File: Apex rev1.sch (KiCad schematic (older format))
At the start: 17 parts, among them J1 OLED, SW1 SW_PUSH, SW2 Rotary_Encoder, U1 AT90USB1286-MU, Y1 8MHz

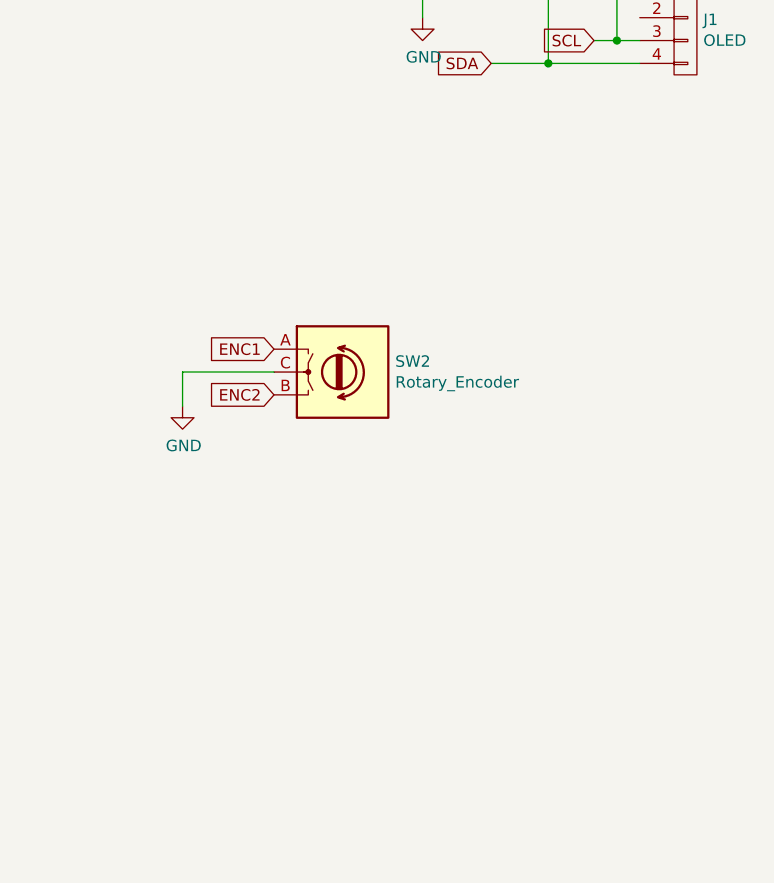
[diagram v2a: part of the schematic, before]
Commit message: Associate FP
added debounce to encoder. finalized footrpint association.
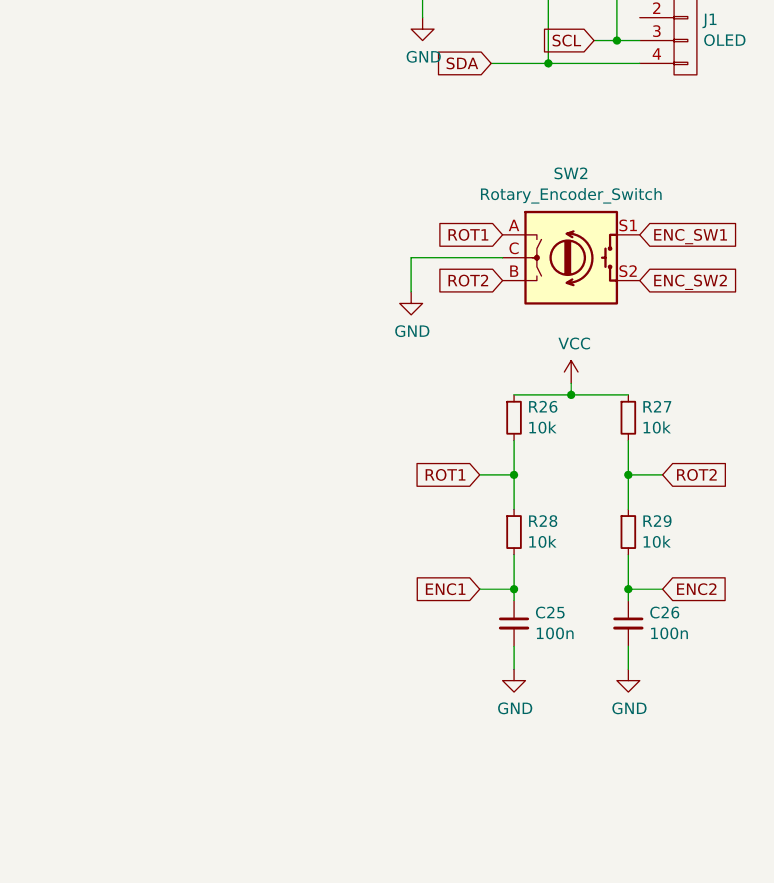
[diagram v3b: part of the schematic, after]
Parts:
- removed SW2: Rotary_Encoder, symbol Device:Rotary_Encoder
- added C25, C26: 100n, Capacitor_SMD:C_0805_2012Metric, symbol Device:C_Small
- added R26, R27, R28, R29: 10k, 1_Keyboard Footprints:R_0603, symbol Device:R_Small
- added SW2: Rotary_Encoder_Switch, 1_Keyboard Footprints:RotaryEncoder_EC11, symbol Device:Rotary_Encoder_Switch
- J1: footprint (none) -> hub_keyboard:128X32_I2C_OLED
- R1, R2, R3, R4: footprint (none) -> 1_Keyboard Footprints:R_0603
- SW1: footprint (none) -> 1_Keyboard Footprints:SKQG-1155865
- Y1: footprint (none) -> Crystal:Crystal_SMD_0603-2Pin_6.0x3.5mm
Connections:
- net ENC1: now also C25.1, R28.2
- net ENC2: now also C26.1, R29.2
- net GND: now also C25.2, C26.2, R26.1, R27.1, SW2.C
- new net ENC_SW1: SW2.S1
- new net ENC_SW2: SW2.S2
- new net ROT1: R26.2, R28.1, SW2.A
- new net ROT2: R27.2, R29.1, SW2.B
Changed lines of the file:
@@
 F 0 "R3" H 8321 1546 50  0000 L CNN
 F 1 "10k" H 8321 1455 50  0000 L CNN
-F 2 "" H 8250 1500 60  0001 C CNN
+F 2 "1_Keyboard Footprints:R_0603" H 8250 1500 60  0001 C CNN
 F 3 "" H 8250 1500 60  0000 C CNN
 	1    8250 1500
@@
 F 0 "SW1" H 7800 2005 50  0000 C CNN
 F 1 "SW_PUSH" H 7800 1914 50  0000 C CNN
-F 2 "" H 7800 1750 60  0001 C CNN
+F 2 "1_Keyboard Footprints:SKQG-1155865" H 7800 1750 60  0001 C CNN
 F 3 "" H 7800 1750 60  0000 C CNN
 	1    7800 1750
@@
 F 0 "Y1" V 7904 2181 50  0000 L CNN
 F 1 "8MHz" V 7995 2181 50  0000 L CNN
-F 2 "" H 7950 2050 50  0001 C CNN
+F 2 "Crystal:Crystal_SMD_0603-2Pin_6.0x3.5mm" H 7950 2050 50  0001 C CNN
 F 3 "~" H 7950 2050 50  0001 C CNN
 	1    7950 2050
@@
 F 0 "R4" H 8220 4096 50  0000 L CNN
 F 1 "1k" H 8220 4005 50  0000 L CNN
-F 2 "" V 8080 4050 50  0001 C CNN
+F 2 "1_Keyboard Footprints:R_0603" V 8080 4050 50  0001 C CNN
 F 3 "~" H 8150 4050 50  0001 C CNN
 	1    8150 4050
@@
 F 0 "J1" H 13278 1491 50  0000 L CNN
 F 1 "OLED" H 13278 1400 50  0000 L CNN
-F 2 "" H 13200 1450 50  0001 C CNN
+F 2 "hub_keyboard:128X32_I2C_OLED" H 13200 1450 50  0001 C CNN
 F 3 "" H 13200 1450 50  0000 C CNN
 	1    13200 1450
@@
 F 0 "R1" H 12670 1096 50  0000 L CNN
 F 1 "20k" H 12670 1005 50  0000 L CNN
-F 2 "" V 12530 1050 50  0001 C CNN
+F 2 "1_Keyboard Footprints:R_0603" V 12530 1050 50  0001 C CNN
 F 3 "~" H 12600 1050 50  0001 C CNN
 	1    12600 1050
@@
 F 0 "R2" H 12970 1096 50  0000 L CNN
 F 1 "20k" H 12970 1005 50  0000 L CNN
-F 2 "" V 12830 1050 50  0001 C CNN
+F 2 "1_Keyboard Footprints:R_0603" V 12830 1050 50  0001 C CNN
 F 3 "~" H 12900 1050 50  0001 C CNN
 	1    12900 1050
@@
 	1    0    0    -1
 $EndComp
-$Comp
-L Device:Rotary_Encoder SW2
-U 1 1 5F0786F9
-P 11700 2950
-F 0 "SW2" H 11930 2996 50  0000 L CNN
-F 1 "Rotary_Encoder" H 11930 2905 50  0000 L CNN
-F 2 "" H 11550 3110 50  0001 C CNN
-F 3 "~" H 11700 3210 50  0001 C CNN
-	1    11700 2950
-	1    0    0    -1
-$EndComp
-Text GLabel 11400 2850 0    50   Input ~ 0
-ENC1
-Text GLabel 11400 3050 0    50   Input ~ 0
-ENC2
-Wire Wire Line
-	11400 2950 11000 2950
-Wire Wire Line
-	11000 2950 11000 3100
+Text GLabel 12400 2350 0    50   Input ~ 0
+ROT1
+Text GLabel 12400 2550 0    50   Input ~ 0
+ROT2
+Wire Wire Line
+	12400 2450 12000 2450
+Wire Wire Line
+	12000 2450 12000 2600
 $Comp
 L power:GND #PWR0113
 U 1 1 5F095086
-P 11000 3100
-F 0 "#PWR0113" H 11000 2850 50  0001 C CNN
-F 1 "GND" H 11005 2927 50  0000 C CNN
-F 2 "" H 11000 3100 50  0001 C CNN
-F 3 "" H 11000 3100 50  0001 C CNN
-	1    11000 3100
+P 12000 2600
+F 0 "#PWR0113" H 12000 2350 50  0001 C CNN
+F 1 "GND" H 12005 2427 50  0000 C CNN
+F 2 "" H 12000 2600 50  0001 C CNN
+F 3 "" H 12000 2600 50  0001 C CNN
+	1    12000 2600
 	1    0    0    -1
 $EndComp
@@
 	1    0    0    -1
 $EndComp
+$Comp
+L Device:Rotary_Encoder_Switch SW2
+U 1 1 5F1264AC
+P 12700 2450
+F 0 "SW2" H 12700 2817 50  0000 C CNN
+F 1 "Rotary_Encoder_Switch" H 12700 2726 50  0000 C CNN
+F 2 "1_Keyboard Footprints:RotaryEncoder_EC11" H 12550 2610 50  0001 C CNN
+F 3 "~" H 12700 2710 50  0001 C CNN
+	1    12700 2450
+	1    0    0    -1
+$EndComp
+Text GLabel 13000 2350 2    50   Input ~ 0
+ENC_SW1
+Text GLabel 13000 2550 2    50   Input ~ 0
+ENC_SW2
+$Comp
+L Device:R_Small R26
+U 1 1 5F1291D1
+P 12450 3150
+F 0 "R26" H 12509 3196 50  0000 L CNN
+F 1 "10k" H 12509 3105 50  0000 L CNN
+F 2 "1_Keyboard Footprints:R_0603" H 12450 3150 50  0001 C CNN
+F 3 "~" H 12450 3150 50  0001 C CNN
+	1    12450 3150
+	1    0    0    -1
+$EndComp
+Wire Wire Line
+	12450 3050 12700 3050
+Wire Wire Line
+	12700 3050 12700 3000
+Connection ~ 12700 3050
+Wire Wire Line
+	12700 3050 12950 3050
+$Comp
+L power:VCC #PWR0147
+U 1 1 5F12CEE1
+P 12700 3000
+F 0 "#PWR0147" H 12700 2850 50  0001 C CNN
+F 1 "VCC" H 12715 3173 50  0000 C CNN
+F 2 "" H 12700 3000 50  0001 C CNN
+F 3 "" H 12700 3000 50  0001 C CNN
+	1    12700 3000
+	1    0    0    -1
+$EndComp
+$Comp
+L Device:R_Small R27
+U 1 1 5F12D64F
+P 12950 3150
+F 0 "R27" H 13009 3196 50  0000 L CNN
+F 1 "10k" H 13009 3105 50  0000 L CNN
+F 2 "1_Keyboard Footprints:R_0603" H 12950 3150 50  0001 C CNN
+F 3 "~" H 12950 3150 50  0001 C CNN
+	1    12950 3150
+	1    0    0    -1
+$EndComp
+$Comp
+L Device:R_Small R29
+U 1 1 5F12DB95
+P 12950 3650
+F 0 "R29" H 13009 3696 50  0000 L CNN
+F 1 "10k" H 13009 3605 50  0000 L CNN
+F 2 "1_Keyboard Footprints:R_0603" H 12950 3650 50  0001 C CNN
+F 3 "~" H 12950 3650 50  0001 C CNN
+	1    12950 3650
+	1    0    0    -1
+$EndComp
+$Comp
+L Device:R_Small R28
+U 1 1 5F12E22B
+P 12450 3650
+F 0 "R28" H 12509 3696 50  0000 L CNN
+F 1 "10k" H 12509 3605 50  0000 L CNN
+F 2 "1_Keyboard Footprints:R_0603" H 12450 3650 50  0001 C CNN
+F 3 "~" H 12450 3650 50  0001 C CNN
+	1    12450 3650
+	1    0    0    -1
+$EndComp
+Wire Wire Line
+	12450 3250 12450 3400
+Wire Wire Line
+	12950 3250 12950 3400
+Wire Wire Line
+	12950 3750 12950 3900
+Wire Wire Line
+	12450 3750 12450 3900
+$Comp
+L Device:C_Small C25
+U 1 1 5F132E89
+P 12450 4050
+F 0 "C25" H 12542 4096 50  0000 L CNN
+F 1 "100n" H 12542 4005 50  0000 L CNN
+F 2 "Capacitor_SMD:C_0805_2012Metric" H 12450 4050 50  0001 C CNN
+F 3 "~" H 12450 4050 50  0001 C CNN
+	1    12450 4050
+	1    0    0    -1
+$EndComp
+$Comp
+L Device:C_Small C26
+U 1 1 5F133D98
+P 12950 4050
+F 0 "C26" H 13042 4096 50  0000 L CNN
+F 1 "100n" H 13042 4005 50  0000 L CNN
+F 2 "Capacitor_SMD:C_0805_2012Metric" H 12950 4050 50  0001 C CNN
+F 3 "~" H 12950 4050 50  0001 C CNN
+	1    12950 4050
+	1    0    0    -1
+$EndComp
+Text GLabel 12300 3400 0    50   Input ~ 0
+ROT1
+Text GLabel 13100 3400 2    50   Input ~ 0
+ROT2
+Wire Wire Line
+	12300 3400 12450 3400
+Connection ~ 12450 3400
+Wire Wire Line
+	12450 3400 12450 3550
+Wire Wire Line
+	13100 3400 12950 3400
+Connection ~ 12950 3400
+Wire Wire Line
+	12950 3400 12950 3550
+Wire Wire Line
+	12450 3900 12300 3900
+Connection ~ 12450 3900
+Wire Wire Line
+	12450 3900 12450 3950
+Wire Wire Line
+	12950 3900 13100 3900
+Connection ~ 12950 3900
+Wire Wire Line
+	12950 3900 12950 3950
+Text GLabel 12300 3900 0    50   Input ~ 0
+ENC1
+Text GLabel 13100 3900 2    50   Input ~ 0
+ENC2
+$Comp
+L power:GND #PWR0148
+U 1 1 5F208042
+P 12450 4250
+F 0 "#PWR0148" H 12450 4000 50  0001 C CNN
+F 1 "GND" H 12455 4077 50  0000 C CNN
+F 2 "" H 12450 4250 50  0001 C CNN
+F 3 "" H 12450 4250 50  0001 C CNN
+	1    12450 4250
+	1    0    0    -1
+$EndComp
+Wire Wire Line
+	12450 4150 12450 4250
+Wire Wire Line
+	12950 4150 12950 4250
+$Comp
+L power:GND #PWR0149
+U 1 1 5F20B367
+P 12950 4250
+F 0 "#PWR0149" H 12950 4000 50  0001 C CNN
+F 1 "GND" H 12955 4077 50  0000 C CNN
+F 2 "" H 12950 4250 50  0001 C CNN
+F 3 "" H 12950 4250 50  0001 C CNN
+	1    12950 4250
+	1    0    0    -1
+$EndComp
